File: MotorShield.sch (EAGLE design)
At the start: 88 parts, among them IC1 OPA4340E, IC2 OPA4340E

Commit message: named connector blocks and ADC
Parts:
- renumbered U$1 to X2, U$16 to X9, U$2 to X3, U$3 to X4, U$34 to X1, U$4 to X5, U$5 to X, U$58 to IC3, U$6 to X7, U$7 to X8

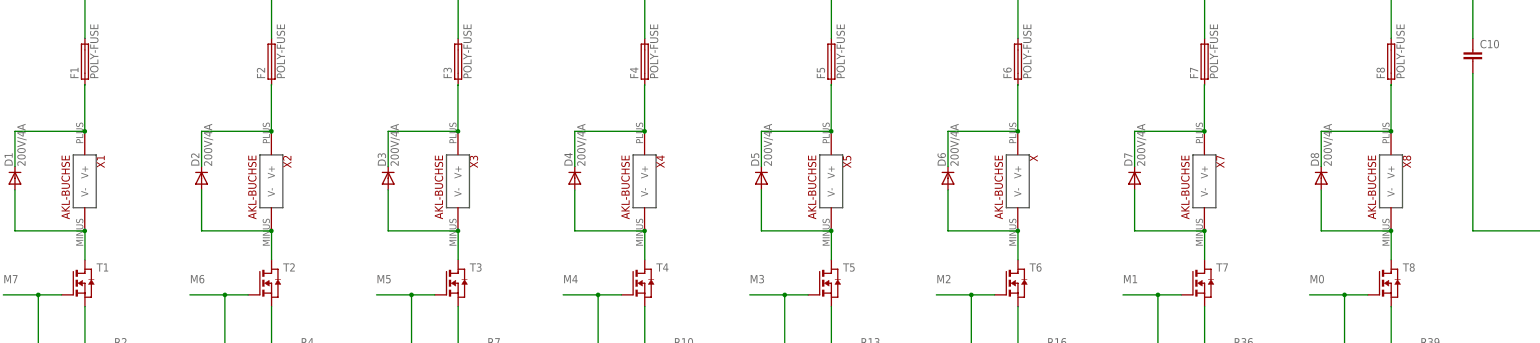
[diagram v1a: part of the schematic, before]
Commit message: added LEDs that signalize active output to close IUNO-TDM/MotorShield#6
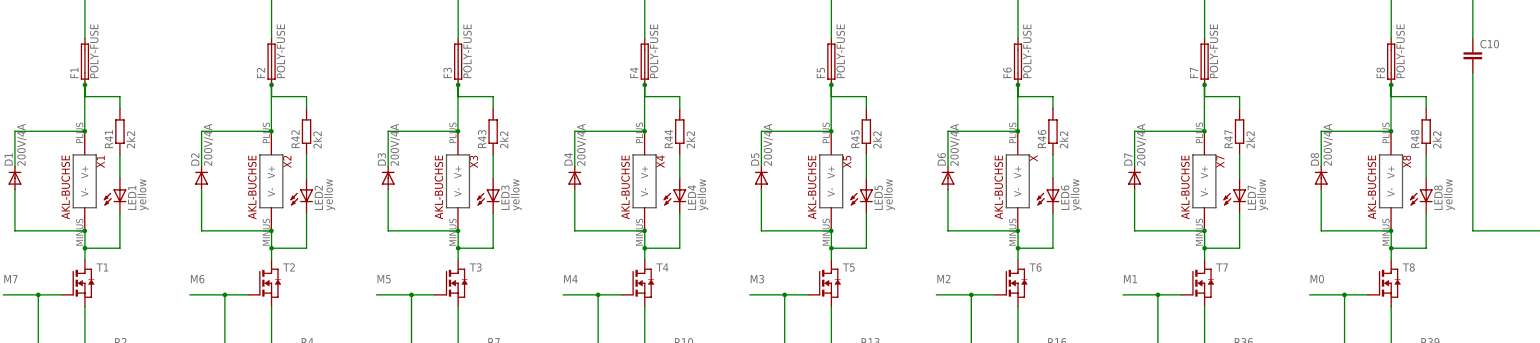
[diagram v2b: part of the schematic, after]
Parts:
- added LED1, LED2, LED3, LED4, LED5, LED6, LED7, LED8: yellow, led:LEDCHIP-LED0603
- added R41, R42, R43, R44, R45, R46, R47, R48: 2k2, rcl:R-EU_R0603
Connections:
- new net N$16: LED1.A, R41.1
- new net N$19: LED2.A, R42.1
- new net N$20: LED3.A, R43.1
- new net N$21: LED5.A, R45.1
- new net N$23: LED4.A, R44.1
- new net N$24: LED6.A, R46.1
- new net N$25: LED7.A, R47.1
- new net N$30: LED8.A, R48.1
- net 24V/1A: now also R41.2
- net N$10: now also LED2.C
- net N$12: now also R43.2
- net N$13: now also R42.2
- net N$17: now also LED3.C
- net N$2: now also LED1.C
- net N$26: now also LED4.C
- net N$38: now also LED5.C
- net N$4: now also R48.2
- net N$45: now also LED6.C
- net N$5: now also R47.2
- net N$51: now also LED7.C
- net N$57: now also LED8.C
- net N$7: now also R46.2
- net N$8: now also R45.2
- net N$9: now also R44.2
